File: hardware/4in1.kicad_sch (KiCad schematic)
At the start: 27 parts, among them J1 SM08B-SRSS-TB, U12 INA186A3IDCKR, U13 LMR54406DBVR, U14 FTC160808S4R7MBCA, U15 TLV76733DRVR

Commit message: Rev 3: 8S rating, input TVS removed
The 3x SMBJ24A are removed. Their 24 V standoff sits below the 33.6 V a full 8S
pack reaches, so they conducted rather than protected. There is no input clamp
now; the 3S-8S rating rests on bench and flight testing on 8S.

README and DESIGN.md updated: 3S-8S, no TVS, and the envelope stated in terms
of the SP40N01GHNK MOSFET (40 V VDSS), the LMR54406DBVR buck (36 V rated, 45 V
absolute maximum, 50 V short transient) and the ~330 A current-sense
full-scale.

ERC and DRC reviewed by the maintainer.

Co-Authored-By: Claude Opus 5 (1M context) <noreply@anthropic.com>
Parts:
- removed D1, D2, D3: SMBJ24A, 4in1ESC-30x30:SMB_L4.5-W3.7-LS5.4-RD, symbol components:SMBJ26A_C908802
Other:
- note added: "4 to 45V, can handle 50V spikes. 8S works 1.1Mhz, 0.6A (plenty for gate driving)"
- note added: "No TVS diodes in Rev3. Too much leakage, clamping above threshold of mosfets meaning they don't do anything anyways. TVS diodes don't work in this case. Testing with them removed showed no difference in voltage spike behavior"
- note removed: "4 to 36V, can handle 50V spikes. TBD on 8S 1.1Mhz, 0.6A (plenty for gate driving)"
- note removed: "SMBJ24A means there will be some leakage at fully charged 6S (25.2V) but voltage clamping gets improved too, will monitor this tradeoff"

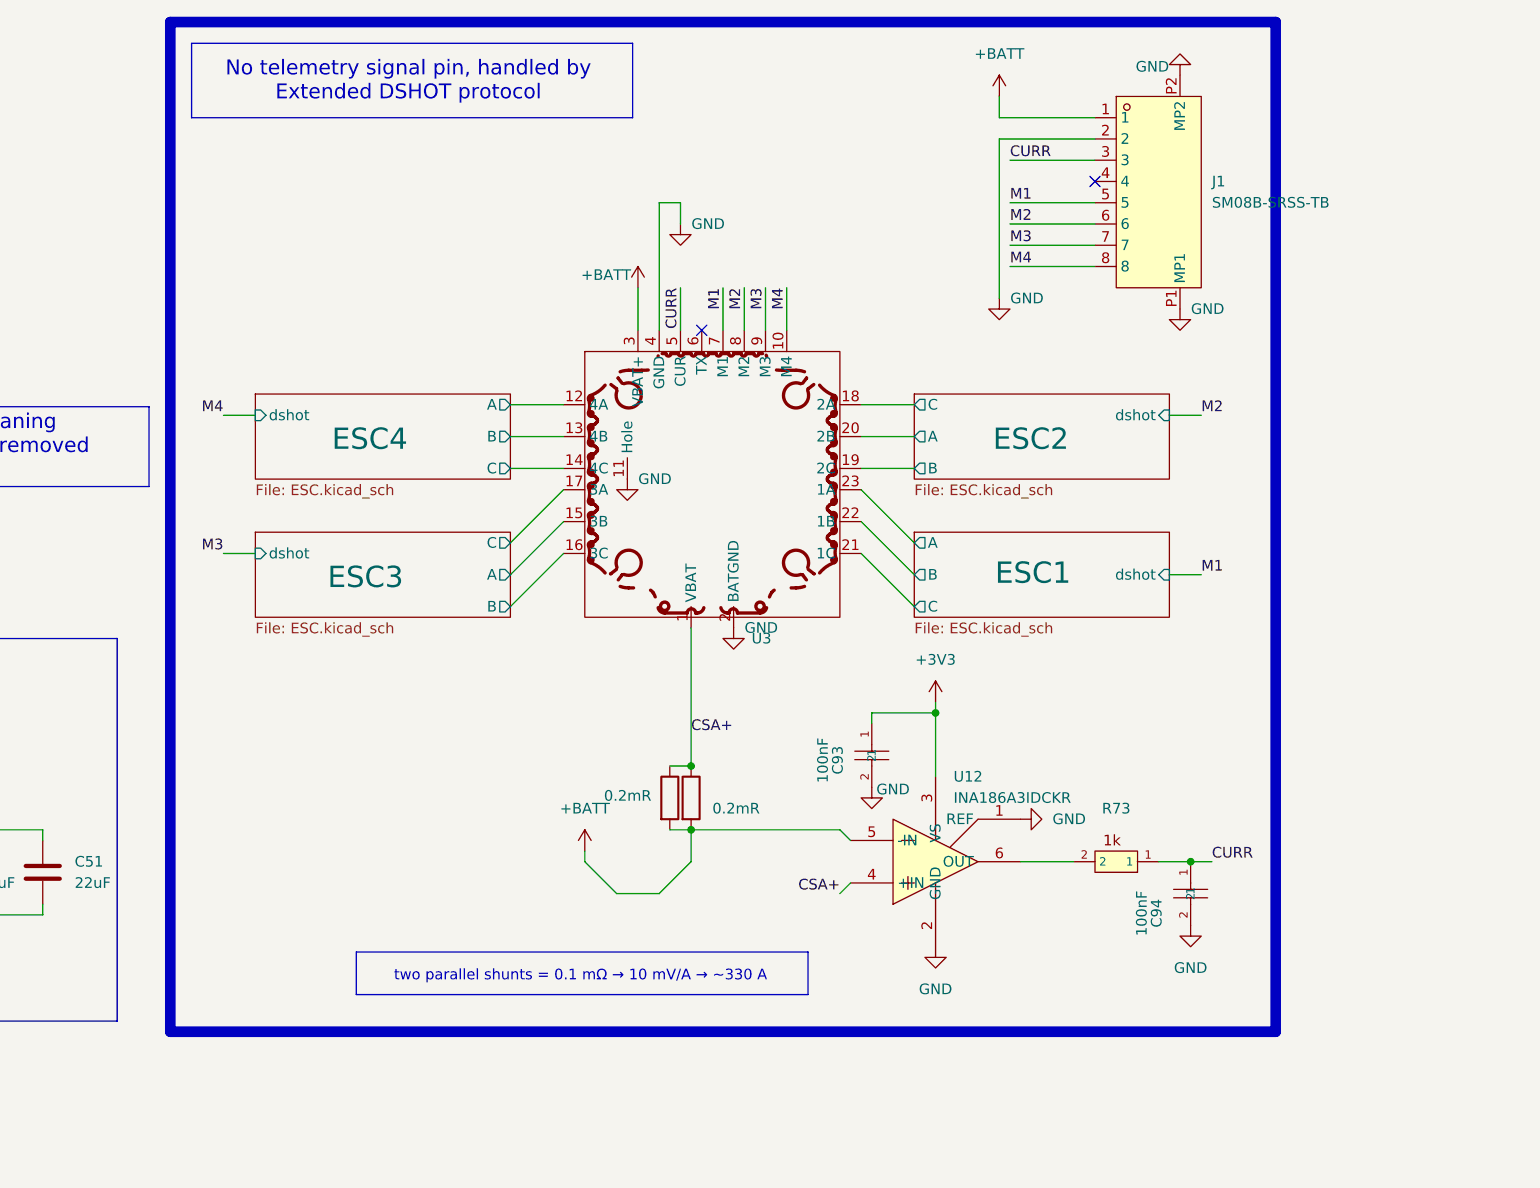
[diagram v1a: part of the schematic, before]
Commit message: CSA input filter: starve the high-side feedthrough before the amplifier
/CURR was garbage below full throttle, measured 2026-08-21 on the 20x20
sibling: bus common-mode at 24-54 kHz rectifies in the INA186 front end,
whose CMRR is ~80 dB there against an 8 mV full-scale signal.

R89/R90 1k (C270365) in each sense leg, C40/C41 100n 50V (C307331) to
ground, C42 1u (C7500381) across the amplifier inputs. Worst-case SPICE
(1% R, 10% C mismatch, 10 Vpp CM at 50 kHz): common-mode at the pins
drops 300x, converted differential ripple 2.8 mVpp, DC gain error
-0.08 percent. C42 does the load-bearing work: without it the C40/C41
mismatch converts CM to 59 mVpp of differential, 7x full scale. Values
hold with the CM caps derated to 30 percent at full bus bias because
C42 sits at zero bias. Per TI SBOS318B section 8.1.3, input filtering
costs nothing at the INA186's pA bias currents.

Gates: ERC errors all pre-existing benign pin-type classes, new
subcircuit connectivity verified against the netlist; DRC 0 errors,
parity at the documented 89 board-only items, copper sliver pre-exists
at HEAD and HEAD's connection_width warning is gone; model preflight
0 blocking.

Acceptance test: ESC-04 mid-throttle i_a vs clamp sweep on this rev.

Co-Authored-By: Claude Fable 5 <noreply@anthropic.com>
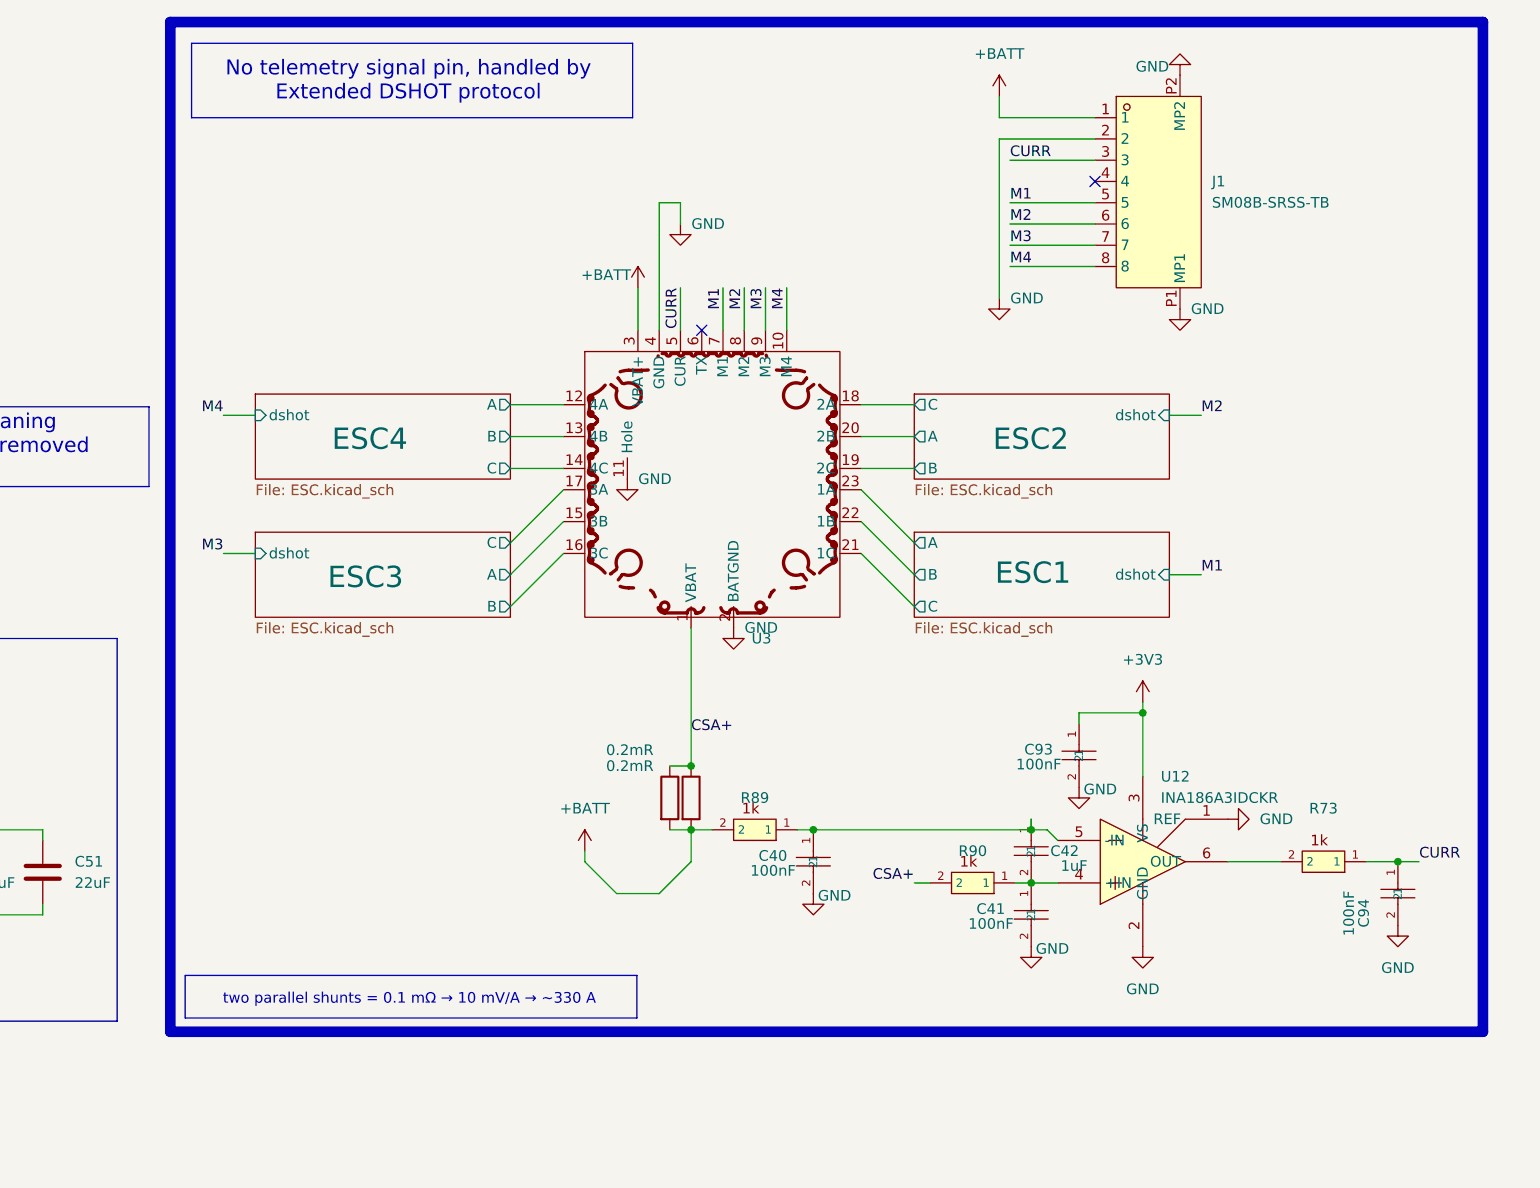
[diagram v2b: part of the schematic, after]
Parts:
- added C40, C41: 100nF, Capacitor_SMD:C_0402_WIDE, symbol ESCLibrary:GRM033R61C104KE84D
- added C42: 1uF, 4in1ESC-30x30:C_0402_1005Metric, symbol ESCLibrary:GRM033R61C104KE84D
- added R89, R90: 1k, Capacitor_SMD:C_0201_0603Metric, symbol components:0201_1kR
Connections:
- net +BATT: now also R89.2; no longer U12.5 (-IN)
- net CSA+: now also R90.2; no longer U12.4 (+IN)
- net GND: now also C40.2, C41.2
- new net: C41.1, C42.2, R90.1, U12.4 (+IN)
- new net: C40.1, C42.1, R89.1, U12.5 (-IN)
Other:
- moved on the sheet: C93, C94, R73, U12
